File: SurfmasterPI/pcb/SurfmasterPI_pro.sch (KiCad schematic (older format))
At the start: 73 parts, among them P1 CLICK_SW, P2 PHONES, P3 BATT_CONN, P4 POWER_SW, P5 THRES, P6 GAIN, P7 COIL, Q1 MPSA13, Q2 IRF9640, Q3 2N3906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

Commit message: Some changes.
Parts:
- removed D2: 1N755, Discret:DO-35, symbol ZENER
- removed P1: CLICK_SW, Pin_Headers:Pin_Header_Straight_1x02, symbol CONN_01X02
- removed R5: 22K, Resistors_ThroughHole:Resistor_Horizontal_RM10mm, symbol R
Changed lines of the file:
@@
-$EndComp
-$Comp
-L CONN_01X02 P1
-U 1 1 57C09B1B
-P 9950 6800
-F 0 "P1" H 9950 6950 50  0000 C CNN
-F 1 "CLICK_SW" V 10050 6800 50  0000 C CNN
-F 2 "Pin_Headers:Pin_Header_Straight_1x02" H 9950 6800 50  0001 C CNN
-F 3 "" H 9950 6800 50  0000 C CNN
-	1    9950 6800
-	-1   0    0    1
-$EndComp
-$Comp
-L ZENER D2
-U 1 1 57C09D39
-P 10200 6350
-F 0 "D2" H 10200 6450 50  0000 C CNN
-F 1 "1N755" H 10200 6250 50  0000 C CNN
-F 2 "Discret:DO-35" H 10200 6350 50  0001 C CNN
-F 3 "" H 10200 6350 50  0000 C CNN
-	1    10200 6350
-	0    1    1    0
-$EndComp
-$Comp
-L R R5
-U 1 1 57C0A529
-P 10200 7200
-F 0 "R5" V 10280 7200 50  0000 C CNN
-F 1 "22K" V 10200 7200 50  0000 C CNN
-F 2 "Resistors_ThroughHole:Resistor_Horizontal_RM10mm" V 10130 7200 50  0001 C CNN
-F 3 "" H 10200 7200 50  0000 C CNN
-	1    10200 7200
-	-1   0    0    1
 $EndComp
 $Comp
@@
 $EndComp
 $Comp
-L +BATT #PWR025
-U 1 1 57C246FD
-P 10200 6100
-F 0 "#PWR025" H 10200 5950 50  0001 C CNN
-F 1 "+BATT" H 10200 6240 50  0000 C CNN
-F 2 "" H 10200 6100 50  0000 C CNN
-F 3 "" H 10200 6100 50  0000 C CNN
-	1    10200 6100
-	1    0    0    -1
-$EndComp
-$Comp
 L +BATT #PWR026
 U 1 1 57C479C0
@@
 	8550 8200 8550 7900
 Wire Wire Line
-	10200 6750 10150 6750
-Wire Wire Line
-	10200 6550 10200 6750
-Wire Wire Line
 	12950 7550 12950 5500
 Wire Wire Line
@@
 	3000 1600 3000 4200
 Wire Wire Line
-	10200 6150 10200 6100
-Wire Wire Line
 	10750 2000 10750 1950
 Wire Wire Line
@@
 Connection ~ 11900 4350
 Wire Wire Line
-	10200 7550 10200 7350
-Connection ~ 10200 7550
-Wire Wire Line
 	9650 3400 9700 3400
 Wire Wire Line
@@
 NoConn ~ 4650 7600
 Wire Wire Line
-	10150 6850 10200 6850
-Wire Wire Line
-	10200 6850 10200 7050
-Wire Wire Line
 	8750 2050 8700 2050

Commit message: Added patent. Changed TO-92 footprint to compact one.
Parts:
- Q1, Q3, U3: footprint TO_SOT_Packages_THT:TO-92_Rugged -> TO_SOT_Packages_THT:TO-92_Molded_Narrow
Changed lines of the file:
@@
 $EndComp
 $Comp
-L +BATT #PWR026
+L +BATT #PWR025
 U 1 1 57C479C0
 P 14150 6350
-F 0 "#PWR026" H 14150 6200 50  0001 C CNN
+F 0 "#PWR025" H 14150 6200 50  0001 C CNN
 F 1 "+BATT" H 14150 6490 50  0000 C CNN
 F 2 "" H 14150 6350 50  0000 C CNN
@@
 $EndComp
 $Comp
-L GND #PWR027
+L GND #PWR026
 U 1 1 57C4DADC
 P 14150 8400
-F 0 "#PWR027" H 14150 8150 50  0001 C CNN
+F 0 "#PWR026" H 14150 8150 50  0001 C CNN
 F 1 "GND" H 14150 8250 50  0000 C CNN
 F 2 "" H 14150 8400 50  0000 C CNN
@@
 $EndComp
 $Comp
-L GND #PWR028
+L GND #PWR027
 U 1 1 57C5107E
 P 14600 7200
-F 0 "#PWR028" H 14600 6950 50  0001 C CNN
+F 0 "#PWR027" H 14600 6950 50  0001 C CNN
 F 1 "GND" H 14600 7050 50  0000 C CNN
 F 2 "" H 14600 7200 50  0000 C CNN
@@
 F 0 "Q3" H 3950 1650 50  0000 R CNN
 F 1 "2N3906" H 4250 1550 50  0000 R CNN
-F 2 "TO_SOT_Packages_THT:TO-92_Rugged" H 3850 1700 50  0001 C CNN
+F 2 "TO_SOT_Packages_THT:TO-92_Molded_Narrow" H 3850 1700 50  0001 C CNN
 F 3 "" H 3650 1600 50  0000 C CNN
 	1    3650 1600
@@
 $EndComp
 $Comp
-L GND #PWR029
+L GND #PWR028
 U 1 1 57C56DF2
 P 5350 1350
-F 0 "#PWR029" H 5350 1100 50  0001 C CNN
+F 0 "#PWR028" H 5350 1100 50  0001 C CNN
 F 1 "GND" H 5350 1200 50  0000 C CNN
 F 2 "" H 5350 1350 50  0000 C CNN
@@
 F 0 "Q1" H 14000 7750 50  0000 C CNN
 F 1 "MPSA13" H 13800 7400 50  0000 C CNN
-F 2 "TO_SOT_Packages_THT:TO-92_Rugged" H 14000 7500 50  0001 C CNN
+F 2 "TO_SOT_Packages_THT:TO-92_Molded_Narrow" H 14000 7500 50  0001 C CNN
 F 3 "" H 14000 7500 50  0000 C CNN
 	1    14000 7550
@@
 F 0 "U3" H 1600 5150 50  0000 C CNN
 F 1 "LM78L05ACZ" H 1800 5150 50  0000 L CNN
-F 2 "TO_SOT_Packages_THT:TO-92_Rugged" H 1800 5050 50  0001 C CIN
+F 2 "TO_SOT_Packages_THT:TO-92_Molded_Narrow" H 1800 5050 50  0001 C CIN
 F 3 "" H 1800 4950 50  0000 C CNN
 	1    1800 4950
@@
 $EndComp
 $Comp
-L +5V #PWR030
+L +5V #PWR029
 U 1 1 57C5395E
 P 6950 3950
-F 0 "#PWR030" H 6950 3800 50  0001 C CNN
+F 0 "#PWR029" H 6950 3800 50  0001 C CNN
 F 1 "+5V" H 6950 4090 50  0000 C CNN
 F 2 "" H 6950 3950 50  0000 C CNN
@@
 $EndComp
 $Comp
-L +5V #PWR031
+L +5V #PWR030
 U 1 1 57C53A98
 P 6950 5250
-F 0 "#PWR031" H 6950 5100 50  0001 C CNN
+F 0 "#PWR030" H 6950 5100 50  0001 C CNN
 F 1 "+5V" H 6950 5390 50  0000 C CNN
 F 2 "" H 6950 5250 50  0000 C CNN
@@
 $EndComp
 $Comp
-L +5V #PWR032
+L +5V #PWR031
 U 1 1 57C5F6BC
 P 8450 5150
-F 0 "#PWR032" H 8450 5000 50  0001 C CNN
+F 0 "#PWR031" H 8450 5000 50  0001 C CNN
 F 1 "+5V" H 8450 5290 50  0000 C CNN
 F 2 "" H 8450 5150 50  0000 C CNN
@@
 $EndComp
 $Comp
-L GND #PWR033
+L GND #PWR032
 U 1 1 57C6BF81
 P 12150 2250
-F 0 "#PWR033" H 12150 2000 50  0001 C CNN
+F 0 "#PWR032" H 12150 2000 50  0001 C CNN
 F 1 "GND" H 12150 2100 50  0000 C CNN
 F 2 "" H 12150 2250 50  0000 C CNN
@@
 $EndComp
 $Comp
-L GND #PWR034
+L GND #PWR033
 U 1 1 57C7412A
 P 11250 4750
-F 0 "#PWR034" H 11250 4500 50  0001 C CNN
+F 0 "#PWR033" H 11250 4500 50  0001 C CNN
 F 1 "GND" H 11250 4600 50  0000 C CNN
 F 2 "" H 11250 4750 50  0000 C CNN
@@
 $EndComp
 $Comp
-L PWR_FLAG #FLG035
+L PWR_FLAG #FLG034
 U 1 1 57CBC361
 P 1200 6800
-F 0 "#FLG035" H 1200 6895 50  0001 C CNN
+F 0 "#FLG034" H 1200 6895 50  0001 C CNN
 F 1 "PWR_FLAG" H 1200 6980 50  0000 C CNN
 F 2 "" H 1200 6800 50  0000 C CNN
@@
 $EndComp
 $Comp
-L GND #PWR036
+L GND #PWR035
 U 1 1 57CBCB57
 P 1200 7000
-F 0 "#PWR036" H 1200 6750 50  0001 C CNN
+F 0 "#PWR035" H 1200 6750 50  0001 C CNN
 F 1 "GND" H 1200 6850 50  0000 C CNN
 F 2 "" H 1200 7000 50  0000 C CNN
@@
 $EndComp
 $Comp
-L +BATT #PWR037
+L +BATT #PWR036
 U 1 1 57CBE233
 P 1900 6750
-F 0 "#PWR037" H 1900 6600 50  0001 C CNN
+F 0 "#PWR036" H 1900 6600 50  0001 C CNN
 F 1 "+BATT" H 1900 6890 50  0000 C CNN
 F 2 "" H 1900 6750 50  0000 C CNN
@@
 $EndComp
 $Comp
-L PWR_FLAG #FLG038
+L PWR_FLAG #FLG037
 U 1 1 57CBE36D
 P 2400 6750
-F 0 "#FLG038" H 2400 6845 50  0001 C CNN
+F 0 "#FLG037" H 2400 6845 50  0001 C CNN
 F 1 "PWR_FLAG" H 2400 6930 50  0000 C CNN
 F 2 "" H 2400 6750 50  0000 C CNN

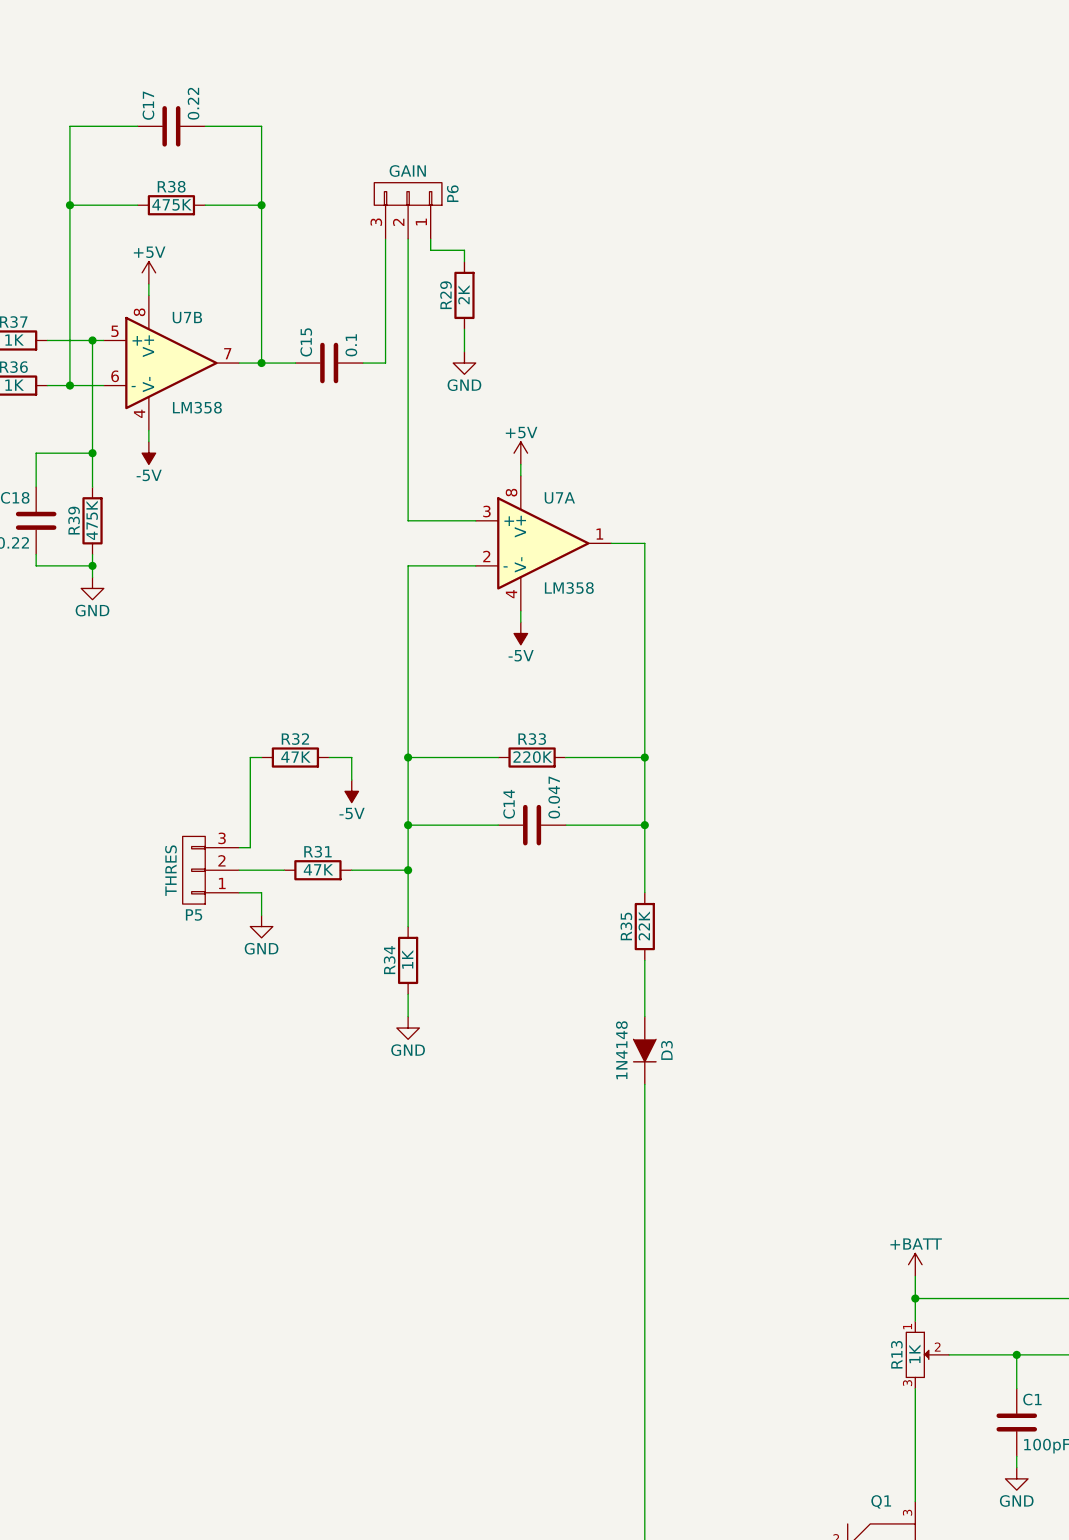
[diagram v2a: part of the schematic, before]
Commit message: Finished first version of PCB layout for pro.
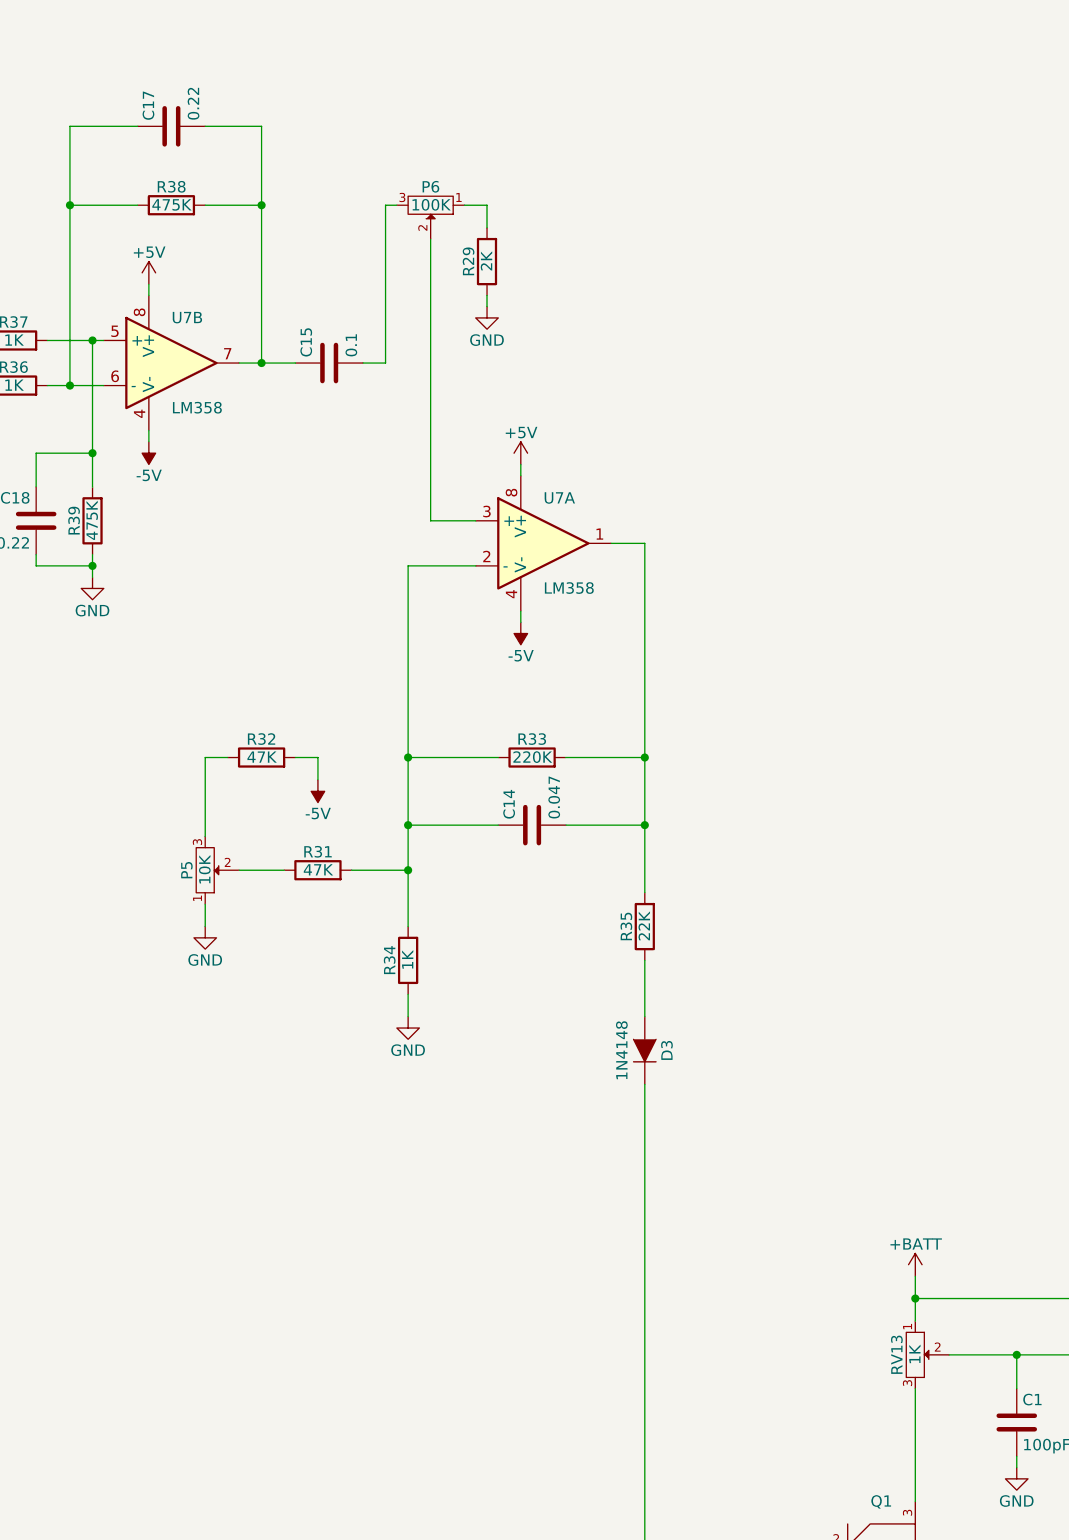
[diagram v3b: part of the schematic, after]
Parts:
- removed P5: THRES, Pin_Headers:Pin_Header_Straight_1x03, symbol CONN_01X03
- removed P6: GAIN, Pin_Headers:Pin_Header_Straight_1x03, symbol CONN_01X03
- removed R13: 1K, Potentiometers:Potentiometer_VishaySpectrol-Econtrim-Type36k, symbol POT
- added P5: 10K, Potentiometers:Potentiometer_WirePads_Small, symbol POT
- added P6: 100K, Potentiometers:Potentiometer_WirePads_Small, symbol POT
- added RV13: 1K, Potentiometers:Potentiometer_WirePads_Small, symbol POT
- R30, R43: footprint Potentiometers:Potentiometer_VishaySpectrol-Econtrim-Type36k -> Potentiometers:Potentiometer_Trimmer-Suntan-TSR-3386P
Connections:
- net +BATT: now also RV13.1
- net GND: now also P5.1
- net at U7.3 (+): now also P6.2
- net at C15.2: now also P6.3
- net at R29.2: now also P6.1
- net at R31.1: now also P5.2
- net at R32.1: now also P5.3
- net at C1.1, P2.2 (P2): now also RV13.2
- net at Q1.3: now also RV13.3
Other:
- moved on the sheet: R29, R32
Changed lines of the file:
@@
 F 0 "R43" H 7350 1320 50  0000 C CNN
 F 1 "100K" H 7350 1400 50  0000 C CNN
-F 2 "Potentiometers:Potentiometer_VishaySpectrol-Econtrim-Type36k" H 7350 1400 50  0001 C CNN
+F 2 "Potentiometers:Potentiometer_Trimmer-Suntan-TSR-3386P" H 7350 1400 50  0001 C CNN
 F 3 "" H 7350 1400 50  0000 C CNN
 	1    7350 1400
@@
 $EndComp
 $Comp
-L -5V #PWR55
+L -5V #PWR47
 U 1 1 57BF46C0
 P 12400 3450
-F 0 "#PWR55" H 12400 3550 50  0001 C CNN
+F 0 "#PWR47" H 12400 3550 50  0001 C CNN
 F 1 "-5V" H 12400 3600 50  0000 C CNN
 F 2 "" H 12400 3450 50  0000 C CNN
@@
 $EndComp
 $Comp
-L CONN_01X03 P6
-U 1 1 57BF57EE
-P 11900 1550
-F 0 "P6" H 11900 1750 50  0000 C CNN
-F 1 "GAIN" V 12000 1550 50  0000 C CNN
-F 2 "Pin_Headers:Pin_Header_Straight_1x03" H 11900 1550 50  0001 C CNN
-F 3 "" H 11900 1550 50  0000 C CNN
-	1    11900 1550
-	0    1    -1   0
-$EndComp
-$Comp
 L R R33
 U 1 1 57BF5C46
@@
 $EndComp
 $Comp
-L CONN_01X03 P5
-U 1 1 57BF65DD
-P 10950 4550
-F 0 "P5" H 10950 4750 50  0000 C CNN
-F 1 "THRES" V 11050 4550 50  0000 C CNN
-F 2 "Pin_Headers:Pin_Header_Straight_1x03" H 10950 4550 50  0001 C CNN
-F 3 "" H 10950 4550 50  0000 C CNN
-	1    10950 4550
-	-1   0    0    1
-$EndComp
-$Comp
 L R R29
 U 1 1 57BF6FF0
-P 12150 2000
-F 0 "R29" V 12230 2000 50  0000 C CNN
-F 1 "2K" V 12150 2000 50  0000 C CNN
-F 2 "Resistors_ThroughHole:Resistor_Horizontal_RM10mm" V 12080 2000 50  0001 C CNN
-F 3 "" H 12150 2000 50  0000 C CNN
-	1    12150 2000
+P 12250 1850
+F 0 "R29" V 12330 1850 50  0000 C CNN
+F 1 "2K" V 12250 1850 50  0000 C CNN
+F 2 "Resistors_ThroughHole:Resistor_Horizontal_RM10mm" V 12180 1850 50  0001 C CNN
+F 3 "" H 12250 1850 50  0000 C CNN
+	1    12250 1850
 	-1   0    0    1
 $EndComp
@@
 L R R32
 U 1 1 57BF7304
-P 11400 4050
-F 0 "R32" V 11480 4050 50  0000 C CNN
-F 1 "47K" V 11400 4050 50  0000 C CNN
-F 2 "Resistors_ThroughHole:Resistor_Horizontal_RM10mm" V 11330 4050 50  0001 C CNN
-F 3 "" H 11400 4050 50  0000 C CNN
-	1    11400 4050
+P 11250 4050
+F 0 "R32" V 11330 4050 50  0000 C CNN
+F 1 "47K" V 11250 4050 50  0000 C CNN
+F 2 "Resistors_ThroughHole:Resistor_Horizontal_RM10mm" V 11180 4050 50  0001 C CNN
+F 3 "" H 11250 4050 50  0000 C CNN
+	1    11250 4050
 	0    -1   -1   0
 $EndComp
@@
 $EndComp
 $Comp
-L -5V #PWR51
+L -5V #PWR43
 U 1 1 57BF78AB
-P 11650 4150
-F 0 "#PWR51" H 11650 4250 50  0001 C CNN
-F 1 "-5V" H 11650 4300 50  0000 C CNN
-F 2 "" H 11650 4150 50  0000 C CNN
-F 3 "" H 11650 4150 50  0000 C CNN
-	1    11650 4150
+P 11500 4150
+F 0 "#PWR43" H 11500 4250 50  0001 C CNN
+F 1 "-5V" H 11500 4300 50  0000 C CNN
+F 2 "" H 11500 4150 50  0000 C CNN
+F 3 "" H 11500 4150 50  0000 C CNN
+	1    11500 4150
 	-1   0    0    1
 $EndComp
@@
 F 0 "R30" H 4900 3970 50  0000 C CNN
 F 1 "10K" H 4900 4050 50  0000 C CNN
-F 2 "Potentiometers:Potentiometer_VishaySpectrol-Econtrim-Type36k" H 4900 4050 50  0001 C CNN
+F 2 "Potentiometers:Potentiometer_Trimmer-Suntan-TSR-3386P" H 4900 4050 50  0001 C CNN
 F 3 "" H 4900 4050 50  0000 C CNN
 	1    4900 4050
@@
 $EndComp
 $Comp
-L -5V #PWR37
+L -5V #PWR38
 U 1 1 57C18E1A
 P 9700 3500
-F 0 "#PWR37" H 9700 3600 50  0001 C CNN
+F 0 "#PWR38" H 9700 3600 50  0001 C CNN
 F 1 "-5V" H 9700 3650 50  0000 C CNN
 F 2 "" H 9700 3500 50  0000 C CNN
@@
 $EndComp
 $Comp
-L -5V #PWR45
+L -5V #PWR41
 U 1 1 57C1992F
 P 10750 2650
-F 0 "#PWR45" H 10750 2750 50  0001 C CNN
+F 0 "#PWR41" H 10750 2750 50  0001 C CNN
 F 1 "-5V" H 10750 2800 50  0000 C CNN
 F 2 "" H 10750 2650 50  0000 C CNN
@@
 $EndComp
 $Comp
-L -5V #PWR29
+L -5V #PWR31
 U 1 1 57C1C1E5
 P 8200 7800
-F 0 "#PWR29" H 8200 7900 50  0001 C CNN
+F 0 "#PWR31" H 8200 7900 50  0001 C CNN
 F 1 "-5V" H 8200 7950 50  0000 C CNN
 F 2 "" H 8200 7800 50  0000 C CNN
@@
 	1    14150 6350
 	1    0    0    -1
-$EndComp
-$Comp
-L POT R13
-U 1 1 57C491F3
-P 14150 6700
-F 0 "R13" H 14150 6620 50  0000 C CNN
-F 1 "1K" H 14150 6700 50  0000 C CNN
-F 2 "Potentiometers:Potentiometer_VishaySpectrol-Econtrim-Type36k" H 14150 6700 50  0001 C CNN
-F 3 "" H 14150 6700 50  0000 C CNN
-	1    14150 6700
-	0    1    1    0
 $EndComp
 $Comp
@@
 $EndComp
 $Comp
-L -5V #PWR36
+L -5V #PWR28
 U 1 1 57C50D7F
 P 7900 2400
-F 0 "#PWR36" H 7900 2500 50  0001 C CNN
+F 0 "#PWR28" H 7900 2500 50  0001 C CNN
 F 1 "-5V" H 7900 2550 50  0000 C CNN
 F 2 "" H 7900 2400 50  0000 C CNN
@@
 $EndComp
 $Comp
-L -5V #PWR34
+L -5V #PWR33
 U 1 1 57C5F7F6
 P 8450 5950
-F 0 "#PWR34" H 8450 6050 50  0001 C CNN
+F 0 "#PWR33" H 8450 6050 50  0001 C CNN
 F 1 "-5V" H 8450 6100 50  0000 C CNN
 F 2 "" H 8450 5950 50  0000 C CNN
@@
 L GND #PWR032
 U 1 1 57C6BF81
-P 12150 2250
-F 0 "#PWR032" H 12150 2000 50  0001 C CNN
-F 1 "GND" H 12150 2100 50  0000 C CNN
-F 2 "" H 12150 2250 50  0000 C CNN
-F 3 "" H 12150 2250 50  0000 C CNN
-	1    12150 2250
+P 12250 2050
+F 0 "#PWR032" H 12250 1800 50  0001 C CNN
+F 1 "GND" H 12250 1900 50  0000 C CNN
+F 2 "" H 12250 2050 50  0000 C CNN
+F 3 "" H 12250 2050 50  0000 C CNN
+	1    12250 2050
 	1    0    0    -1
 $EndComp
@@
 L GND #PWR033
 U 1 1 57C7412A
-P 11250 4750
-F 0 "#PWR033" H 11250 4500 50  0001 C CNN
-F 1 "GND" H 11250 4600 50  0000 C CNN
-F 2 "" H 11250 4750 50  0000 C CNN
-F 3 "" H 11250 4750 50  0000 C CNN
-	1    11250 4750
+P 11000 4800
+F 0 "#PWR033" H 11000 4550 50  0001 C CNN
+F 1 "GND" H 11000 4650 50  0000 C CNN
+F 2 "" H 11000 4800 50  0000 C CNN
+F 3 "" H 11000 4800 50  0000 C CNN
+	1    11000 4800
 	1    0    0    -1
 $EndComp
@@
 Connection ~ 11250 2300
 Wire Wire Line
-	11700 2300 11800 2300
+	11800 2300 11700 2300
 Wire Wire Line
 	12600 4050 12950 4050
@@
 Connection ~ 12950 4050
 Wire Wire Line
-	12150 1800 12150 1850
-Wire Wire Line
-	11250 4750 11250 4650
-Wire Wire Line
-	11250 4650 11150 4650
-Wire Wire Line
-	11150 4450 11200 4450
-Wire Wire Line
-	11200 4450 11200 4050
-Wire Wire Line
-	11200 4050 11250 4050
-Wire Wire Line
-	11550 4050 11650 4050
-Wire Wire Line
-	11650 4050 11650 4150
+	12250 1600 12250 1700
+Wire Wire Line
+	11000 4800 11000 4800
+Wire Wire Line
+	11000 4800 11000 4700
+Wire Wire Line
+	11000 4400 11000 4050
+Wire Wire Line
+	11000 4050 11100 4050
+Wire Wire Line
+	11400 4050 11500 4050
+Wire Wire Line
+	11500 4050 11500 4150
 Wire Wire Line
 	11150 4550 11350 4550
@@
 	7350 1200 7150 1200
 Wire Wire Line
-	12150 2150 12150 2250
-Wire Wire Line
-	11800 2300 11800 1750
-Wire Wire Line
-	11900 1750 11900 3000
-Wire Wire Line
-	11900 3000 12200 3000
-Wire Wire Line
-	12150 1800 12000 1800
-Wire Wire Line
-	12000 1800 12000 1750
+	12250 2000 12250 2050
+Wire Wire Line
+	11800 1600 11800 2300
+Wire Wire Line
+	12000 1750 12000 3000
+Wire Wire Line
+	12000 3000 12200 3000
+Wire Wire Line
+	12250 1600 12150 1600
 Wire Wire Line
 	11650 4550 11900 4550
@@
 Wire Wire Line
 	8750 2050 8700 2050
+$Comp
+L POT RV13
+U 1 1 57C3D6A4
+P 14150 6700
+F 0 "RV13" H 14150 6620 50  0000 C CNN
+F 1 "1K" H 14150 6700 50  0000 C CNN
+F 2 "Potentiometers:Potentiometer_WirePads_Small" H 14150 6700 50  0001 C CNN
+F 3 "" H 14150 6700 50  0000 C CNN
+F 4 "VOL" H 14150 6700 60  0001 C CNN "Function"
+	1    14150 6700
+	0    1    1    0
+$EndComp
+$Comp
+L POT P5
+U 1 1 57C3E8E0
+P 11000 4550
+F 0 "P5" H 11000 4470 50  0000 C CNN
+F 1 "10K" H 11000 4550 50  0000 C CNN
+F 2 "Potentiometers:Potentiometer_WirePads_Small" H 11000 4550 50  0001 C CNN
+F 3 "" H 11000 4550 50  0000 C CNN
+F 4 "THRES" H 11000 4550 60  0001 C CNN "Function"
+	1    11000 4550
+	0    1    -1   0
+$EndComp
+$Comp
+L POT P6
+U 1 1 57C42127
+P 12000 1600
+F 0 "P6" H 12000 1520 50  0000 C CNN
+F 1 "100K" H 12000 1600 50  0000 C CNN
+F 2 "Potentiometers:Potentiometer_WirePads_Small" H 12000 1600 50  0001 C CNN
+F 3 "" H 12000 1600 50  0000 C CNN
+F 4 "GAIN" H 12000 1600 60  0001 C CNN "Function"
+	1    12000 1600
+	-1   0    0    1
+$EndComp
+Wire Wire Line
+	11800 1600 11850 1600
 $EndSCHEMATC
